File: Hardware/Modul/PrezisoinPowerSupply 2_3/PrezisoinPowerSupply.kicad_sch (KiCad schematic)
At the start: 184 parts, among them J1 Supply, J2 Conn_01x03_Pin, J3 Conn_02x05_Odd_Even, J6 Output, J7 USB_C_Receptacle, J8 Conn_01x08_Socket, K1 EE2-5NU, K3 SANYOU_SRD_Form_C, Q1 IRFP240, Q2 IRFP9240, Q3 MMBT3904, Q4 IRFP9240, Q5 MMBT3904, Q6 MMBT3904, Q7 MMBT3904, Q8 MMBT3904, Q9 IRFP240, U10 OPA4189, U11 OPA4189, U12 OPA189, U15 OPA2192, U16 ATtiny3227-M, U17 TS5A23159RSE, U19 TLV9301xDBV, U2 DG469, U21 ADS1219, U3 ADA4522, U4 CPC1017N, U5 ISO7763FDBQ, U6 CH340C, U7 DAC8564C/D, U8 MCP9700Ax-ETT, U9 MCP9700Ax-ETT

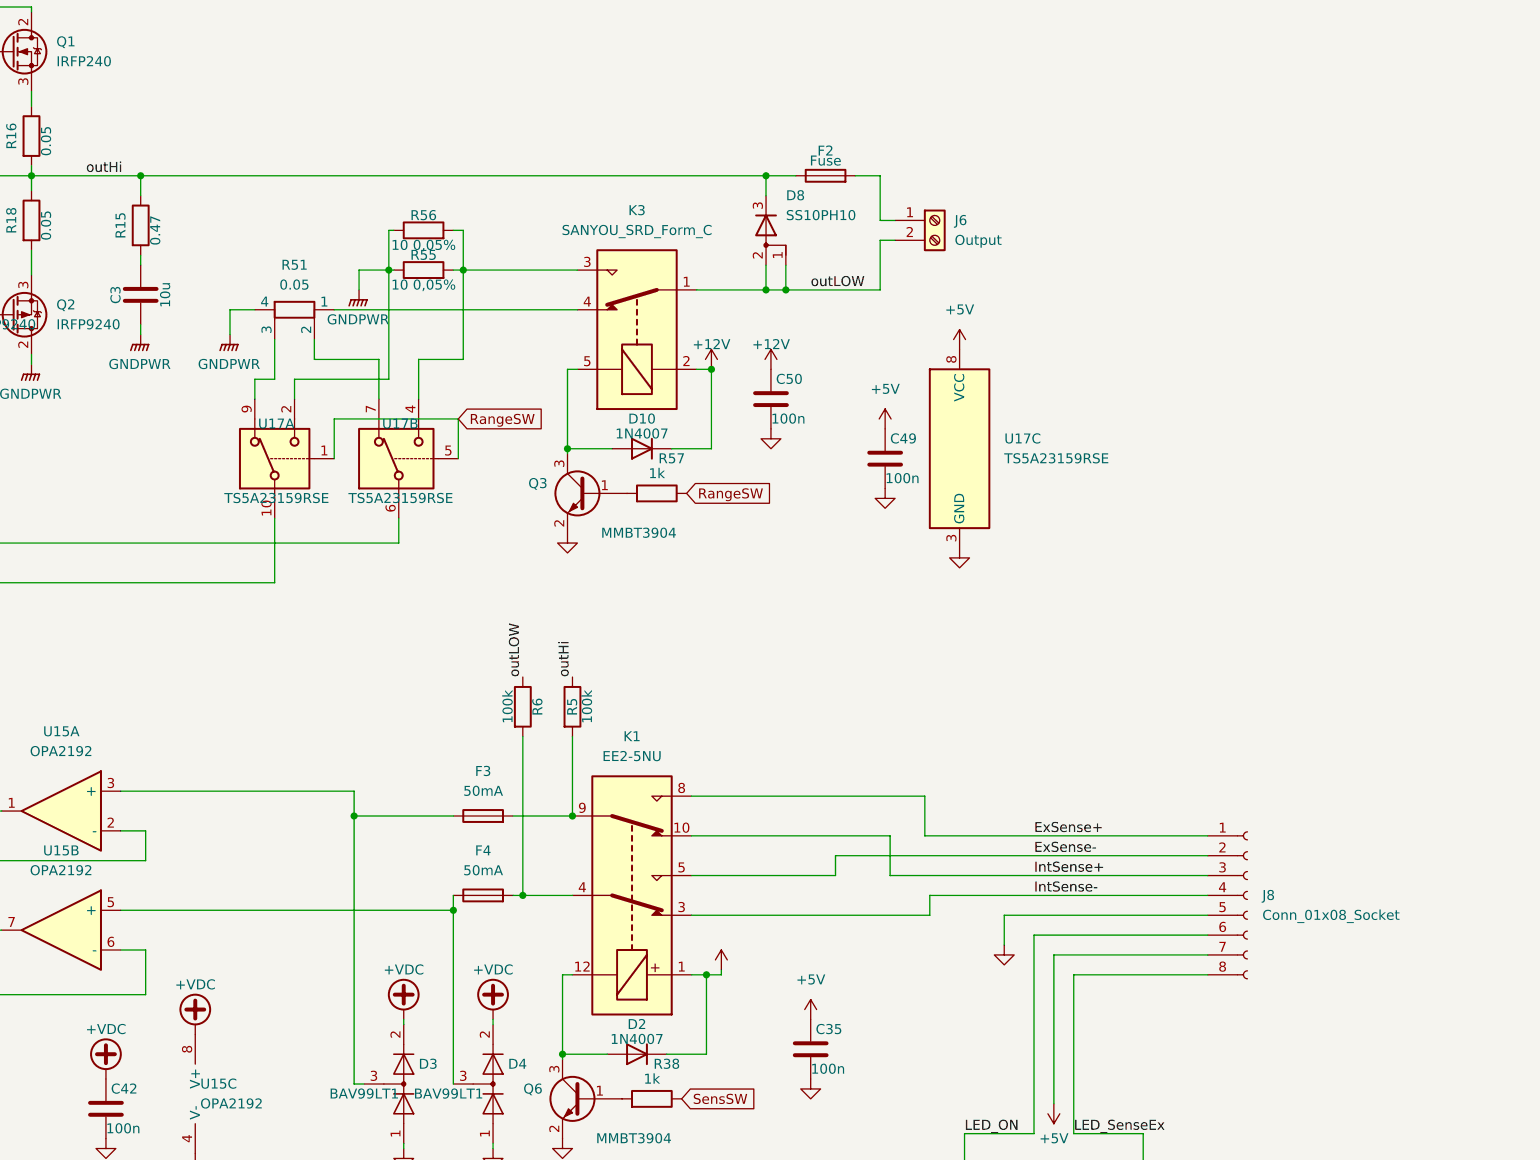
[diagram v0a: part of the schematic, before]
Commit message: hardware Fet Range switching
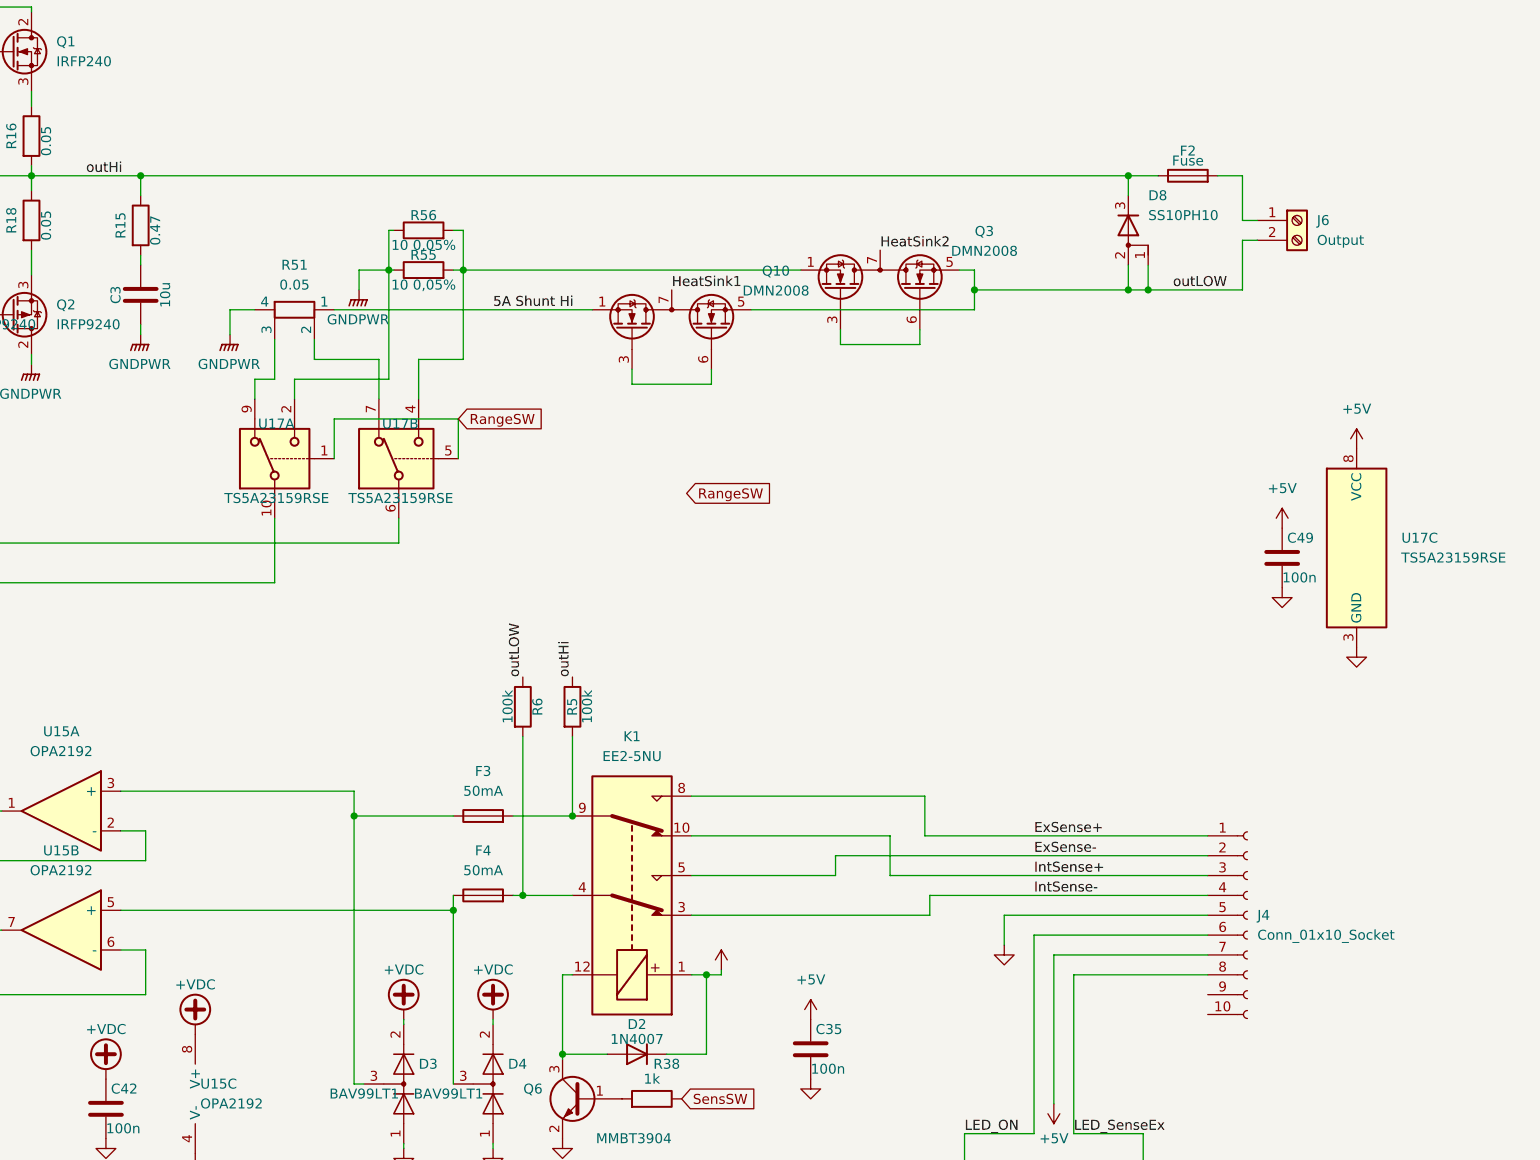
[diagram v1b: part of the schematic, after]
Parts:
- removed C50: 100n, Capacitor_SMD:C_0603_1608Metric, symbol Device:C
- removed D10: 1N4007, Diode_SMD:D_SOD-123F, symbol Device:D
- removed J8: Conn_01x08_Socket, Connector_JST:JST_GH_BM08B-GHS-TBT_1x08-1MP_P1.25mm_Vertical, symbol Connector:Conn_01x08_Socket
- removed K3: SANYOU_SRD_Form_C, Relay_THT:Relay_SPDT_SANYOU_SRD_Series_Form_C, symbol Relay:SANYOU_SRD_Form_C
- removed Q3: MMBT3904, Package_TO_SOT_SMD:SOT-23-3, symbol Transistor_BJT:MMBT3904
- removed R57: 1k, Resistor_SMD:R_0603_1608Metric, symbol Device:R
- added J4: Conn_01x10_Socket, Connector_JST:JST_GH_BM10B-GHS-TBT_1x10-1MP_P1.25mm_Vertical, symbol Connector:Conn_01x10_Socket
- added Q10, Q3: DMN2008, Library:DFN-6-1EP_3x2mm_P0.5mm_EP1.65x1.35mm bearb, symbol SymbolLibary:DMN2008
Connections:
- net +5V: now also J4.7 (Pin_7)
- net ExSense+: now also J4.1 (Pin_1)
- net ExSense-: now also J4.2 (Pin_2)
- net GND: now also J4.5 (Pin_5)
- net IntSense+: now also J4.3 (Pin_3)
- net IntSense-: now also J4.4 (Pin_4)
- net LED_ON: now also J4.6 (Pin_6)
- net LED_SenseEx: now also J4.8 (Pin_8)
- net outLOW: now also Q10.4 (S2), Q10.5 (S2), Q3.4 (S2), Q3.5 (S2)
- net at R55.2, R56.2, U17.4: now also Q3.1 (D1), Q3.2 (D1)
- net 5A Shunt Hi: now reaches R51.1
- net 5A Shunt Hi: now also Q10.1 (D1), Q10.2 (D1)
- new net: Q3.3 (G1), Q3.6 (G1)
- new net: Q10.3 (G1), Q10.6 (G1)
- new net HeatSink1: Q10.7 (S1/D2)
- new net HeatSink2: Q3.7 (S1/D2)
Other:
- moved on the sheet: C49, D8, F2, J6, U17C

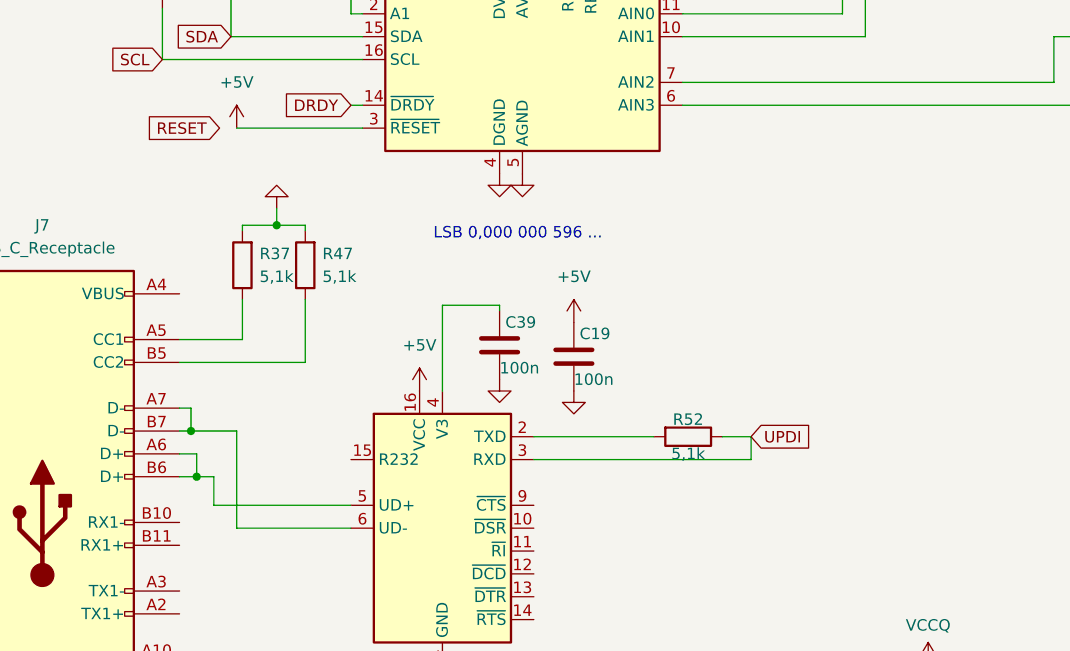
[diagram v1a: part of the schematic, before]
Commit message: rooting and new frontDist
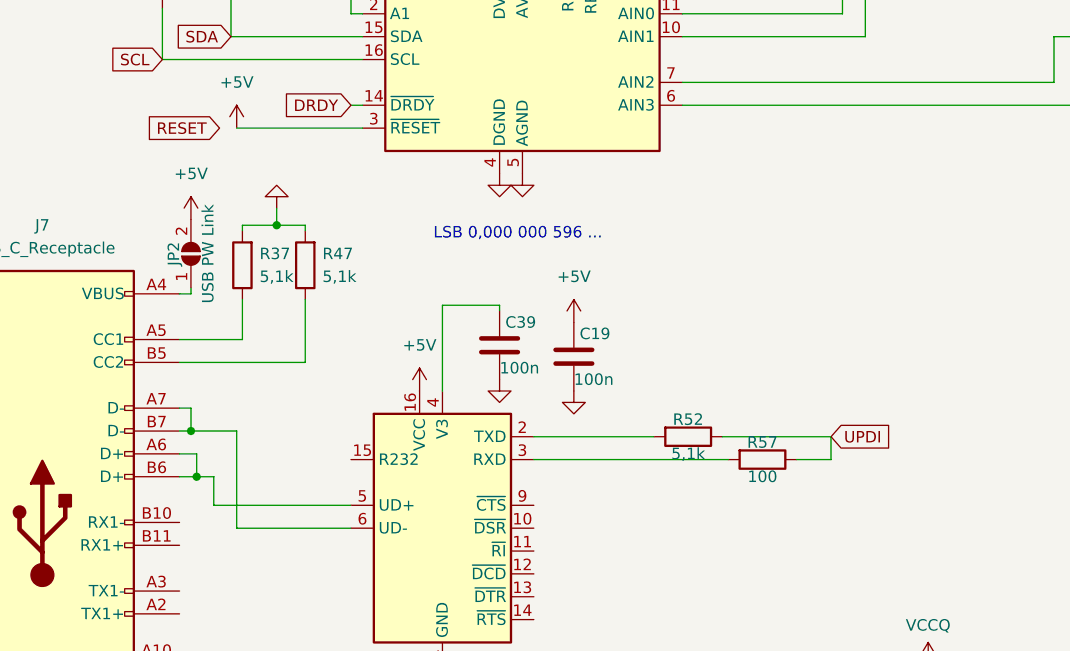
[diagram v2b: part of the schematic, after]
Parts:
- added JP2: USB PW Link, Jumper:SolderJumper-2_P1.3mm_Open_RoundedPad1.0x1.5mm, symbol Jumper:SolderJumper_2_Open
- added R57: 100, Resistor_SMD:R_0603_1608Metric, symbol Device:R
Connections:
- net +5V: now also JP2.2 (B)
- net UPDI: now also R57.1; no longer U6.3 (RXD)
- net at J7.A4 (VBUS), J7.A9 (VBUS), J7.B4 (VBUS)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: now also JP2.1 (A)
- new net: R57.2, U6.3 (RXD)
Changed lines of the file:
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@@
 	(wire
 		(pts
+			(xy 46.99 224.79) (xy 48.26 224.79)
+		)
+		(stroke
+			(width 0)
+			(type default)
+		)
+	)
+	(wire
+		(pts
 			(xy 368.3 94.615) (xy 368.3 92.71)
 		)
@@
 	(wire
 		(pts
+			(xy 48.26 224.79) (xy 48.26 224.155)
+		)
+		(stroke
+			(width 0)
+			(type default)
+		)
+	)
+	(wire
+		(pts
 			(xy 48.895 242.57) (xy 48.895 245.11)
 		)
@@
 	(wire
 		(pts
-			(xy 86.36 243.205) (xy 110.49 243.205)
+			(xy 86.36 243.205) (xy 107.95 243.205)
 		)
 		(stroke
@@
 	(wire
 		(pts
-			(xy 110.49 240.665) (xy 107.315 240.665)
+			(xy 119.38 240.665) (xy 107.315 240.665)
 		)
 		(stroke
@@
 	(wire
 		(pts
+			(xy 115.57 243.205) (xy 119.38 243.205)
+		)
+		(stroke
+			(width 0)
+			(type default)
+		)
+	)
+	(wire
+		(pts
 			(xy 449.58 92.71) (xy 463.55 92.71)
 		)
@@
 	(wire
 		(pts
-			(xy 110.49 243.205) (xy 110.49 240.665)
+			(xy 119.38 243.205) (xy 119.38 240.665)
 		)
 		(stroke
@@
 	(global_label "UPDI"
 		(shape input)
-		(at 110.49 240.665 0)
+		(at 119.38 240.665 0)
 		(fields_autoplaced yes)
 		(effects
@@
 		)
 		(property "Intersheetrefs" "${INTERSHEET_REFS}"
-			(at 117.9505 240.665 0)
+			(at 126.8405 240.665 0)
 			(effects
 				(font
@@
 	)
 	(symbol
+		(lib_id "Jumper:SolderJumper_2_Open")
+		(at 48.26 220.345 90)
+		(unit 1)
+		(exclude_from_sim no)
+		(in_bom yes)
+		(on_board yes)
+		(dnp no)
+		(property "Reference" "JP2"
+			(at 46.355 220.345 0)
+			(effects
+				(font
+					(size 1.27 1.27)
+				)
+			)
+		)
+		(property "Value" "USB PW Link"
+			(at 50.165 220.345 0)
+			(effects
+				(font
+					(size 1.27 1.27)
+				)
+			)
+		)
+		(property "Footprint" "Jumper:SolderJumper-2_P1.3mm_Open_RoundedPad1.0x1.5mm"
+			(at 48.26 220.345 0)
+			(effects
+				(font
+					(size 1.27 1.27)
+				)
+				(hide yes)
+			)
+		)
+		(property "Datasheet" "~"
+			(at 48.26 220.345 0)
+			(effects
+				(font
+					(size 1.27 1.27)
+				)
+				(hide yes)
+			)
+		)
+		(property "Description" "Solder Jumper, 2-pole, open"
+			(at 48.26 220.345 0)
+			(effects
+				(font
+					(size 1.27 1.27)
+				)
+				(hide yes)
+			)
+		)
+		(pin "1"
+		)
+		(pin "2"
+		)
+		(instances
+			(project "PrezisoinPowerSupply"
+				(path "/29e23d3f-5497-45d7-9b61-dc69987ec96b"
+					(reference "JP2")
+					(unit 1)
+				)
+			)
+		)
+	)
+	(symbol
 		(lib_id "Device:Opamp_Quad")
 		(at 494.665 311.785 0)
@@
 	)
 	(symbol
+		(lib_name "+5V_1")
+		(lib_id "power:+5V")
+		(at 48.26 216.535 0)
+		(unit 1)
+		(exclude_from_sim no)
+		(in_bom yes)
+		(on_board yes)
+		(dnp no)
+		(fields_autoplaced yes)
+		(property "Reference" "#PWR0152"
+			(at 48.26 220.345 0)
+			(effects
+				(font
+					(size 1.27 1.27)
+				)
+				(hide yes)
+			)
+		)
+		(property "Value" "+5V"
+			(at 48.26 211.455 0)
+			(effects
+				(font
+					(size 1.27 1.27)
+				)
+			)
+		)
+		(property "Footprint" ""
+			(at 48.26 216.535 0)
+			(effects
+				(font
+					(size 1.27 1.27)
+				)
+				(hide yes)
+			)
+		)
+		(property "Datasheet" ""
+			(at 48.26 216.535 0)
+			(effects
+				(font
+					(size 1.27 1.27)
+				)
+				(hide yes)
+			)
+		)
+		(property "Description" "Power symbol creates a global label with name \"+5V\""
+			(at 48.26 216.535 0)
+			(effects
+				(font
+					(size 1.27 1.27)
+				)
+				(hide yes)
+			)
+		)
+		(pin "1"
+		)
+		(instances
+			(project "PrezisoinPowerSupply"
+				(path "/29e23d3f-5497-45d7-9b61-dc69987ec96b"
+					(reference "#PWR0152")
+					(unit 1)
+				)
+			)
+		)
+	)
+	(symbol
 		(lib_id "power:GND")
 		(at 128.27 138.43 0)
@@
 					(unit 1)
 				)
+			)
+		)
+	)
+	(symbol
+		(lib_id "Device:R")
+		(at 111.76 243.205 270)
+		(unit 1)
+		(exclude_from_sim no)
+		(in_bom yes)
+		(on_board yes)
+		(dnp no)
+		(property "Reference" "R57"
+			(at 111.76 241.3 90)
+			(effects
+				(font
+					(size 1.27 1.27)
+				)
+			)
+		)
+		(property "Value" "100"
+			(at 111.76 245.11 90)
+			(effects
+				(font
+					(size 1.27 1.27)
+				)
+			)
+		)
+		(property "Footprint" "Resistor_SMD:R_0603_1608Metric"
+			(at 111.76 241.427 90)
+			(effects
+				(font
+					(size 1.27 1.27)
+				)
+				(hide yes)
+			)
+		)
+		(property "Datasheet" "~"
+			(at 111.76 243.205 0)
+			(effects
+				(font
+					(size 1.27 1.27)
+				)
+				(hide yes)
+			)
+		)
+		(property "Description" ""
+			(at 111.76 243.205 0)
+			(effects
+				(font
+					(size 1.27 1.27)
+				)
+				(hide yes)
+			)
+		)
+		(pin "1"
+		)
+		(pin "2"
+		)
+		(instances
+			(project "PrezisoinPowerSupply"
+				(path "/29e23d3f-5497-45d7-9b61-dc69987ec96b"
+					(reference "R57")
+					(unit 1)
+				)

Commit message: finalise rooting
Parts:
- added C50, C56: 100n, Capacitor_SMD:C_0603_1608Metric, symbol Device:C
- added U22: SN74LVC1G14DBV, Package_TO_SOT_SMD:SOT-23-5, symbol 74xGxx:SN74LVC1G14DBV
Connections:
- net +5V: now also C56.1, U22.5 (VCC)
- net GND: now also C50.2, C56.2, U22.3 (GND)
- net RangeSW: now also Q3.3 (G1), Q3.6 (G1), U22.2
- net outLOW: now also J6.1 (Pin_1); no longer J6.2 (Pin_2)
- net at J7.A4 (VBUS), J7.A9 (VBUS), J7.B4 (VBUS)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: now also C50.1
- net at F2.2: now also J6.2 (Pin_2); no longer J6.1 (Pin_1)
- net at Q10.3 (G1), Q10.6 (G1): now also U22.4
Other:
- moved on the sheet: C49, R37, R47
